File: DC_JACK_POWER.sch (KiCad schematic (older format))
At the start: 8 parts, among them J1 Jack-DC, U3 NCP1117-5.0_SOT223

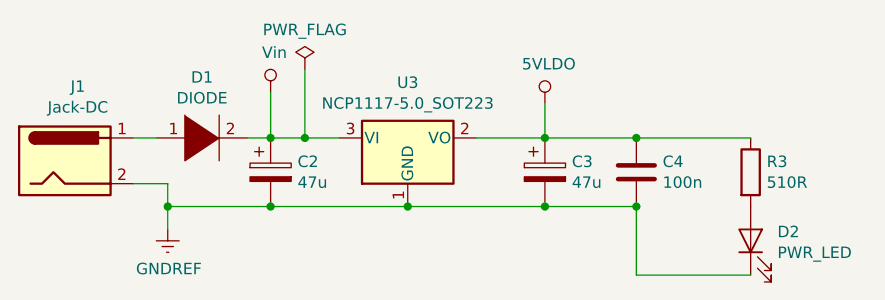
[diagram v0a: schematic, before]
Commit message: Set component footprints, added datasheets, fixed the last DRC error and a couple component values
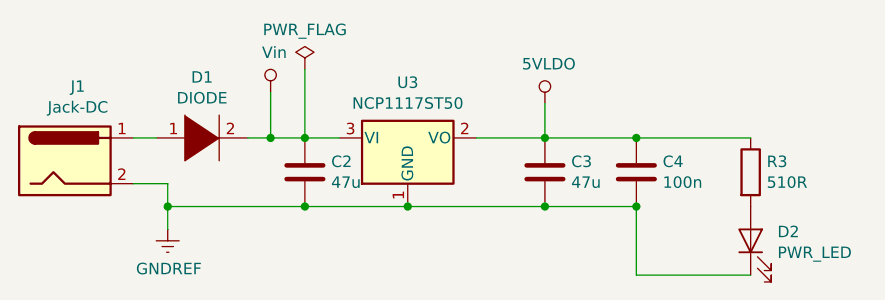
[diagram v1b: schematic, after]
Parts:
- removed C2, C3: 47u, symbol Device:CP
- added C2, C3: 47u, Capacitor_SMD:C_0805_2012Metric, symbol Device:C
- C4: footprint (none) -> Capacitor_SMD:C_0603_1608Metric
- D1: footprint (none) -> Diode_SMD:D_SMF
- D2: footprint (none) -> LED_SMD:LED_0603_1608Metric
- R3: footprint (none) -> Resistor_SMD:R_0603_1608Metric
- U3: value NCP1117-5.0_SOT223 -> NCP1117ST50
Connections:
- net GNDREF: now also C2.2, C3.2
- net at D1.2 (A), U3.3 (VI): now also C2.1
- net at C4.1, R3.1, U3.2 (VO): now also C3.1
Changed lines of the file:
@@
 Wire Wire Line
 	4650 3300 4550 3300
-Wire Wire Line
-	4650 3600 4200 3600
 Connection ~ 4200 3600
 Wire Wire Line
@@
 AR Path="/5EC64FF6/5EC6C3B3" Ref="U3"  Part="1"
 F 0 "U3" H 5250 3542 50  0000 C CNN
-F 1 "NCP1117-5.0_SOT223" H 5250 3451 50  0000 C CNN
+F 1 "NCP1117ST50" H 5250 3451 50  0000 C CNN
 F 2 "Package_TO_SOT_SMD:SOT-223-3_TabPin2" H 5250 3500 50  0001 C CNN
-F 3 "http://www.onsemi.com/pub_link/Collateral/NCP1117-D.PDF" H 5350 3050 50  0001 C CNN
+F 3 "http://www.farnell.com/datasheets/2236912.pdf" H 5350 3050 50  0001 C CNN
 	1    5250 3300
-	1    0    0    -1
-$EndComp
-Wire Wire Line
-	5250 3600 4650 3600
-Connection ~ 4650 3600
-$Comp
-L Device:CP C?
-U 1 1 5EC6C3BB
-P 5850 3450
-AR Path="/5EC6C3BB" Ref="C?"  Part="1"
-AR Path="/5EC64FF6/5EC6C3BB" Ref="C3"  Part="1"
-F 0 "C3" H 5968 3496 50  0000 L CNN
-F 1 "47u" H 5968 3405 50  0000 L CNN
-F 2 "" H 5888 3300 50  0001 C CNN
-F 3 "~" H 5850 3450 50  0001 C CNN
-	1    5850 3450
 	1    0    0    -1
 $EndComp
@@
 F 0 "C4" H 6365 3496 50  0000 L CNN
 F 1 "100n" H 6365 3405 50  0000 L CNN
-F 2 "" H 6288 3300 50  0001 C CNN
-F 3 "~" H 6250 3450 50  0001 C CNN
+F 2 "Capacitor_SMD:C_0603_1608Metric" H 6288 3300 50  0001 C CNN
+F 3 "http://www.farnell.com/datasheets/2739842.pdf" H 6250 3450 50  0001 C CNN
 	1    6250 3450
 	1    0    0    -1
@@
 	5550 3300 5850 3300
 Connection ~ 5850 3300
-Wire Wire Line
-	6250 3600 5850 3600
 Connection ~ 5250 3600
-Connection ~ 5850 3600
-Wire Wire Line
-	5850 3600 5250 3600
 $Comp
 L power_symbols:Vin #PWR?
@@
 F 1 "Jack-DC" H 3807 3634 50  0000 C CNN
 F 2 "" H 3800 3360 50  0001 C CNN
-F 3 "~" H 3800 3360 50  0001 C CNN
+F 3 "http://www.farnell.com/datasheets/317160.pdf" H 3800 3360 50  0001 C CNN
 	1    3750 3400
 	1    0    0    -1
@@
 F 0 "D1" H 4350 3565 50  0000 C CNN
 F 1 "DIODE" H 4350 3474 50  0000 C CNN
-F 2 "" H 4350 3300 50  0001 C CNN
-F 3 "~" H 4350 3300 50  0001 C CNN
+F 2 "Diode_SMD:D_SMF" H 4350 3300 50  0001 C CNN
+F 3 "http://www.farnell.com/datasheets/2050495.pdf" H 4350 3300 50  0001 C CNN
 	1    4350 3300
-	1    0    0    -1
-$EndComp
-$Comp
-L Device:CP C2
-U 1 1 5EC6C3A7
-P 4650 3450
-F 0 "C2" H 4768 3496 50  0000 L CNN
-F 1 "47u" H 4768 3405 50  0000 L CNN
-F 2 "" H 4688 3300 50  0001 C CNN
-F 3 "~" H 4650 3450 50  0001 C CNN
-	1    4650 3450
 	1    0    0    -1
 $EndComp
@@
 F 0 "D2" V 6789 3633 50  0000 R CNN
 F 1 "PWR_LED" V 6698 3633 50  0000 R CNN
-F 2 "" H 6750 3750 50  0001 C CNN
-F 3 "~" H 6750 3750 50  0001 C CNN
+F 2 "LED_SMD:LED_0603_1608Metric" H 6750 3750 50  0001 C CNN
+F 3 "http://www.farnell.com/datasheets/1681524.pdf" H 6750 3750 50  0001 C CNN
 	1    6750 3750
 	0    -1   -1   0
@@
 F 0 "R3" H 6820 3496 50  0000 L CNN
 F 1 "510R" H 6820 3405 50  0000 L CNN
-F 2 "" V 6680 3450 50  0001 C CNN
-F 3 "~" H 6750 3450 50  0001 C CNN
+F 2 "Resistor_SMD:R_0603_1608Metric" V 6680 3450 50  0001 C CNN
+F 3 "http://www.farnell.com/datasheets/2310790.pdf" H 6750 3450 50  0001 C CNN
 	1    6750 3450
 	1    0    0    -1
@@
 	4650 3300 4800 3300
 $Comp
-L power:PWR_FLAG #FLG0102
+L power:PWR_FLAG #FLG03
 U 1 1 5ED962BC
 P 4800 3000
-F 0 "#FLG0102" H 4800 3075 50  0001 C CNN
+F 0 "#FLG03" H 4800 3075 50  0001 C CNN
 F 1 "PWR_FLAG" H 4800 3173 50  0000 C CNN
 F 2 "" H 4800 3000 50  0001 C CNN
@@
 Wire Wire Line
 	5850 3300 6250 3300
+Wire Wire Line
+	5250 3600 5850 3600
+Wire Wire Line
+	4200 3600 4800 3600
+$Comp
+L Device:C C?
+U 1 1 5EC70005
+P 5850 3450
+AR Path="/5EC70005" Ref="C?"  Part="1"
+AR Path="/5EC64FF6/5EC70005" Ref="C3"  Part="1"
+F 0 "C3" H 5965 3496 50  0000 L CNN
+F 1 "47u" H 5965 3405 50  0000 L CNN
+F 2 "Capacitor_SMD:C_0805_2012Metric" H 5888 3300 50  0001 C CNN
+F 3 "http://www.farnell.com/datasheets/2792994.pdf" H 5850 3450 50  0001 C CNN
+	1    5850 3450
+	1    0    0    -1
+$EndComp
+Connection ~ 5850 3600
+Wire Wire Line
+	5850 3600 6250 3600
+$Comp
+L Device:C C?
+U 1 1 5EC701B5
+P 4800 3450
+AR Path="/5EC701B5" Ref="C?"  Part="1"
+AR Path="/5EC64FF6/5EC701B5" Ref="C2"  Part="1"
+F 0 "C2" H 4915 3496 50  0000 L CNN
+F 1 "47u" H 4915 3405 50  0000 L CNN
+F 2 "Capacitor_SMD:C_0805_2012Metric" H 4838 3300 50  0001 C CNN
+F 3 "http://www.farnell.com/datasheets/2792994.pdf" H 4800 3450 50  0001 C CNN
+	1    4800 3450
+	1    0    0    -1
+$EndComp
+Connection ~ 4800 3600
+Wire Wire Line
+	4800 3600 5250 3600
 $EndSCHEMATC

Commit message: Updated the schematic, added missing footprints, started PCB design
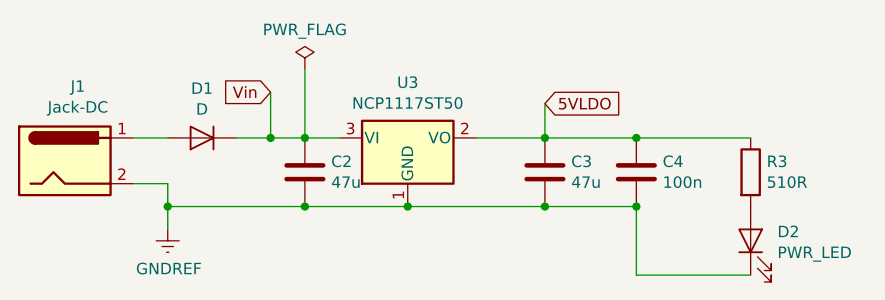
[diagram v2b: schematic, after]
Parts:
- removed D1: DIODE, Diode_SMD:D_SMF, symbol pspice:DIODE
- added D1: D, Diode_SMD:D_SMF, symbol Device:D
- J1: footprint (none) -> footprints:DC_Jack
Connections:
- net at J1.1: now also D1.2 (A)
- net 5VLDO: now reaches C3.1, C4.1, R3.1, U3.2 (VO)
- net Vin: now reaches C2.1, U3.3 (VI)
- net Vin: now also D1.1 (K)
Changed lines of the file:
@@
 Wire Wire Line
 	4200 3500 4200 3600
-Wire Wire Line
-	4050 3300 4150 3300
-Wire Wire Line
-	4650 3300 4550 3300
 Connection ~ 4200 3600
 Wire Wire Line
@@
 	1    0    0    -1
 $EndComp
-Wire Wire Line
-	5550 3300 5850 3300
 Connection ~ 5850 3300
 Connection ~ 5250 3600
-$Comp
-L power_symbols:Vin #PWR?
-U 1 1 5EC7F23B
-P 4650 3100
-AR Path="/5EC7F23B" Ref="#PWR?"  Part="1"
-AR Path="/5EC64FF6/5EC7F23B" Ref="#PWR010"  Part="1"
-F 0 "#PWR010" H 4650 2950 50  0001 C CNN
-F 1 "Vin" H 4667 3273 50  0000 C CNN
-F 2 "" H 4650 3100 50  0001 C CNN
-F 3 "" H 4650 3100 50  0001 C CNN
-	1    4650 3100
-	1    0    0    -1
-$EndComp
 Wire Wire Line
 	5850 3150 5850 3300
@@
 F 0 "J1" H 3807 3725 50  0000 C CNN
 F 1 "Jack-DC" H 3807 3634 50  0000 C CNN
-F 2 "" H 3800 3360 50  0001 C CNN
-F 3 "http://www.farnell.com/datasheets/317160.pdf" H 3800 3360 50  0001 C CNN
+F 2 "footprints:DC_Jack" H 3800 3360 50  0001 C CNN
+F 3 "https://www.sparkfun.com/datasheets/Prototyping/Barrel-Connector-PJ-202A.pdf" H 3800 3360 50  0001 C CNN
 	1    3750 3400
 	1    0    0    -1
@@
 F 3 "" H 4200 3700 50  0001 C CNN
 	1    4200 3700
-	1    0    0    -1
-$EndComp
-$Comp
-L pspice:DIODE D1
-U 1 1 5EC7F236
-P 4350 3300
-F 0 "D1" H 4350 3565 50  0000 C CNN
-F 1 "DIODE" H 4350 3474 50  0000 C CNN
-F 2 "Diode_SMD:D_SMF" H 4350 3300 50  0001 C CNN
-F 3 "http://www.farnell.com/datasheets/2050495.pdf" H 4350 3300 50  0001 C CNN
-	1    4350 3300
-	1    0    0    -1
-$EndComp
-$Comp
-L power_symbols:5VLDO #PWR011
-U 1 1 5EC6C3D6
-P 5850 3150
-F 0 "#PWR011" H 5850 3000 50  0001 C CNN
-F 1 "5VLDO" H 5867 3323 50  0000 C CNN
-F 2 "" H 5850 3150 50  0001 C CNN
-F 3 "" H 5850 3150 50  0001 C CNN
-	1    5850 3150
 	1    0    0    -1
 $EndComp
@@
 Wire Wire Line
 	4800 3600 5250 3600
+$Comp
+L Device:D D1
+U 1 1 5EC8391C
+P 4350 3300
+F 0 "D1" H 4350 3084 50  0000 C CNN
+F 1 "D" H 4350 3175 50  0000 C CNN
+F 2 "Diode_SMD:D_SMF" H 4350 3300 50  0001 C CNN
+F 3 "http://www.farnell.com/datasheets/2050495.pdf" H 4350 3300 50  0001 C CNN
+	1    4350 3300
+	-1   0    0    1
+$EndComp
+Wire Wire Line
+	4050 3300 4200 3300
+Wire Wire Line
+	4500 3300 4650 3300
+Text GLabel 4650 3100 0    50   Input ~ 0
+Vin
+Text GLabel 5850 3150 2    50   Input ~ 0
+5VLDO
+Wire Wire Line
+	5550 3300 5850 3300
 $EndSCHEMATC
